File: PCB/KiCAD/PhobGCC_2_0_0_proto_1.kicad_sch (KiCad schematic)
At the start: 110 parts, among them J1 Conn_01x06_Female, J11 Conn_01x02, J14 Conn_01x06, J15 Conn_01x06, J2 Conn_01x02, J3 Conn_01x02, J4 Conn_01x01, J5 Rumble, J6 Conn_01x06, J8 USB_B_Micro, Q1 Q_NMOS_GSD, Q2 Q_PMOS_GDS, Q3 Q_NMOS_GSD, SW1 A, SW10 Dup, SW11 Dright, SW12 Ddown, SW2 B, SW3 X, SW4 Y, SW5 Start, SW6 L, SW7 R, SW8 Z, SW9 Dleft, U1 MCP3202, U10 DRV5055A3xDBZxQ1, U11 DRV5055A3xDBZxQ1, U12 USBLC6-2P6, U13 USBLC6-2P6, U2 Stickbox_Assembly_Main, U3 MCP3202, U4 DRV5055A3xDBZxQ1, U5 Stickbox_Assembly_CStick, U6 AMS1117-3.3, U7 W25Q128JVS, U8 RP2040, U9 DRV5055A3xDBZxQ1, Y1 Crystal_GND24

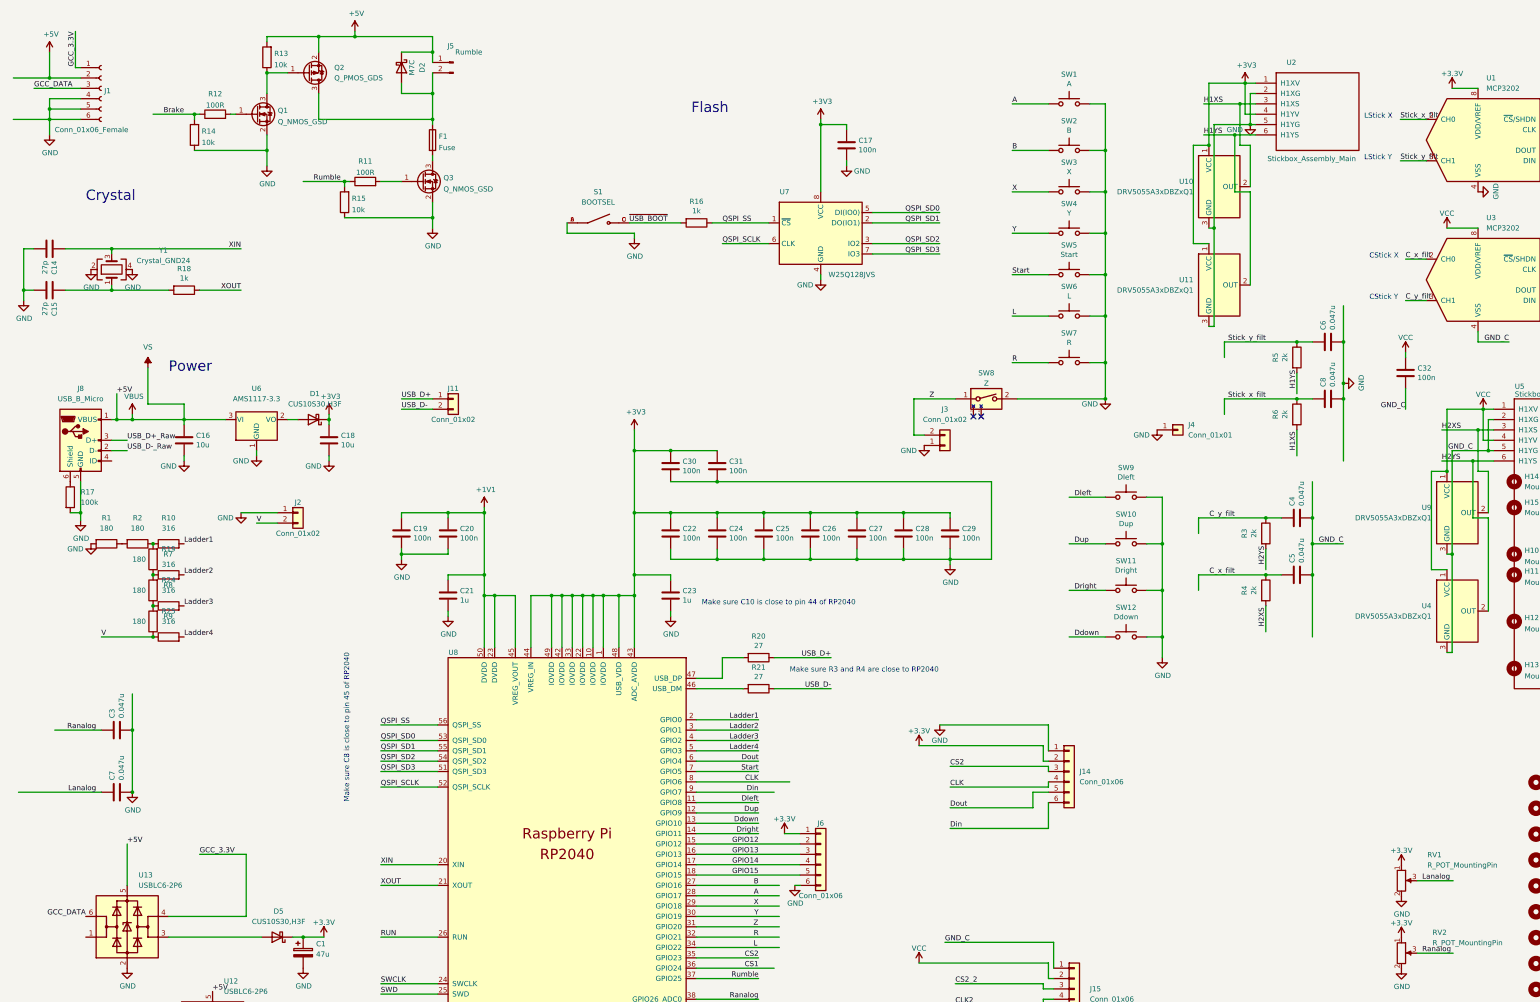
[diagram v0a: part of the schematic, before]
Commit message: Implemented USB-C For Flashing
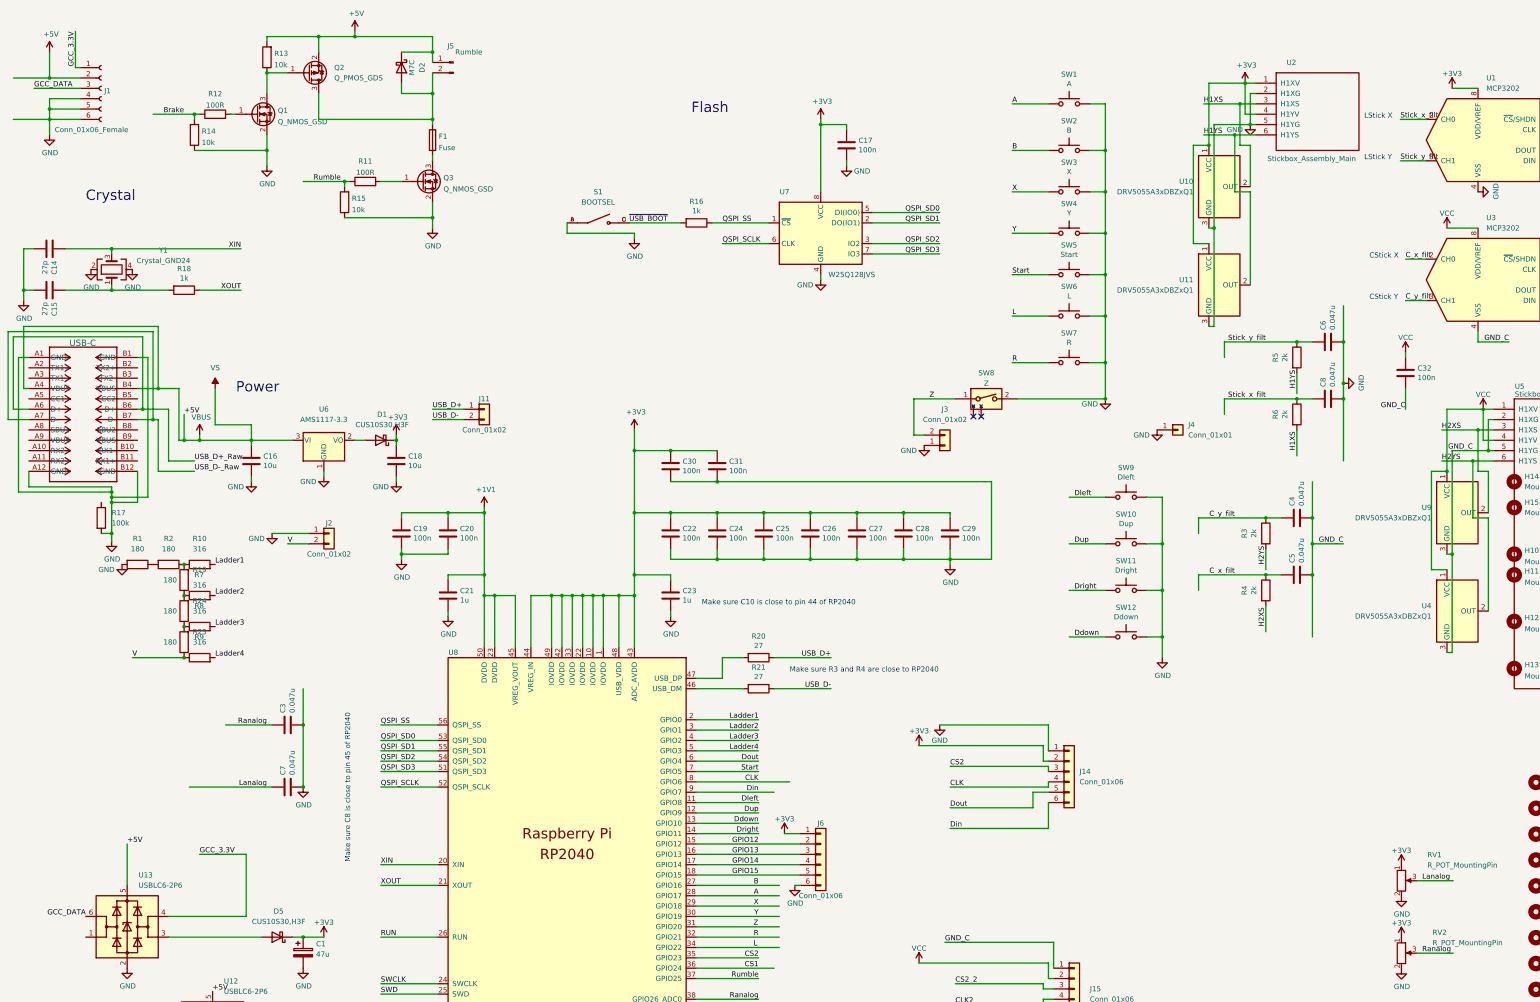
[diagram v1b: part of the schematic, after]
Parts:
- removed J8: USB_B_Micro, PhobGCC_2_0_0_footprints:USB_Micro-B_Amphenol_10118194_Horizontal, symbol Connector:USB_B_Micro
- added J7: USB-C, Connector_USB:USB_C_Receptacle_Molex_105450-0101, symbol Molex USB-C:1054500101
- H1, H10, H11, H12, H13, H14, H15, H2, H3, H4, H5, H6, H7, H8, H9, J1, J11, J14, J15, J2, J3, J4, J5, J6, RV1, RV2, SW1, SW2, SW3, SW4, SW5, SW6, SW7, SW8, U2, U5: now left out of the parts list
- SW10, SW11, SW12, SW9: footprint PhobGCC_2_0_0_footprints:Dpad_Contact_TL3315NF_2_ZigZag -> PhobGCC_2_0_0_footprints:Dpad_Contact_TL3315NF_2
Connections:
- net +5V: now also J7.A4 (VBUS), J7.B4 (VBUS)
- net GND: now also J7.A1 (GND), J7.A12 (GND), J7.B1 (GND), J7.B12 (GND)
- net USB_D+_Raw: now also J7.A6 (D+), J7.B6 (D+)
- net USB_D-_Raw: now also J7.A7 (D-), J7.B7 (D-)
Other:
- moved on the sheet: C16, C18, C3, C7, D1, J11, J2, R1, R10, R17, R19, R2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
